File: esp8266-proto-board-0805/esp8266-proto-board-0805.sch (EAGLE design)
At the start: 13 parts

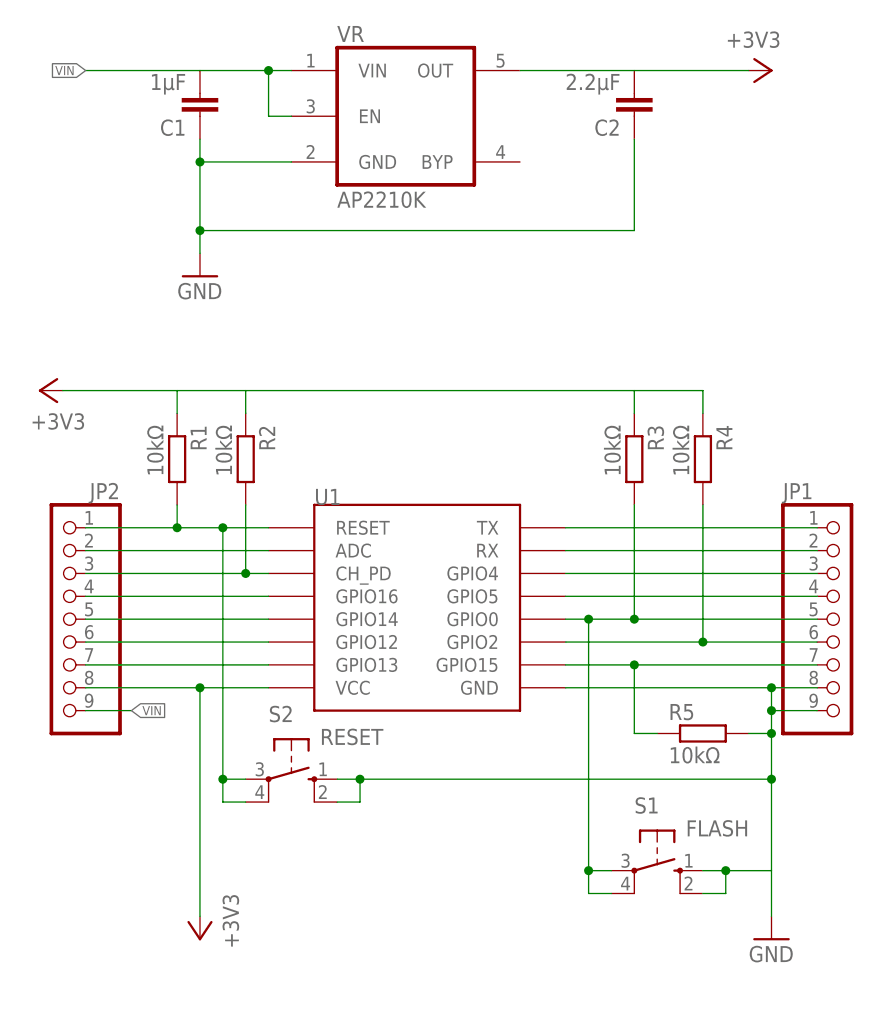
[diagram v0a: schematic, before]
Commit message: reworked 0805 version with better footprint
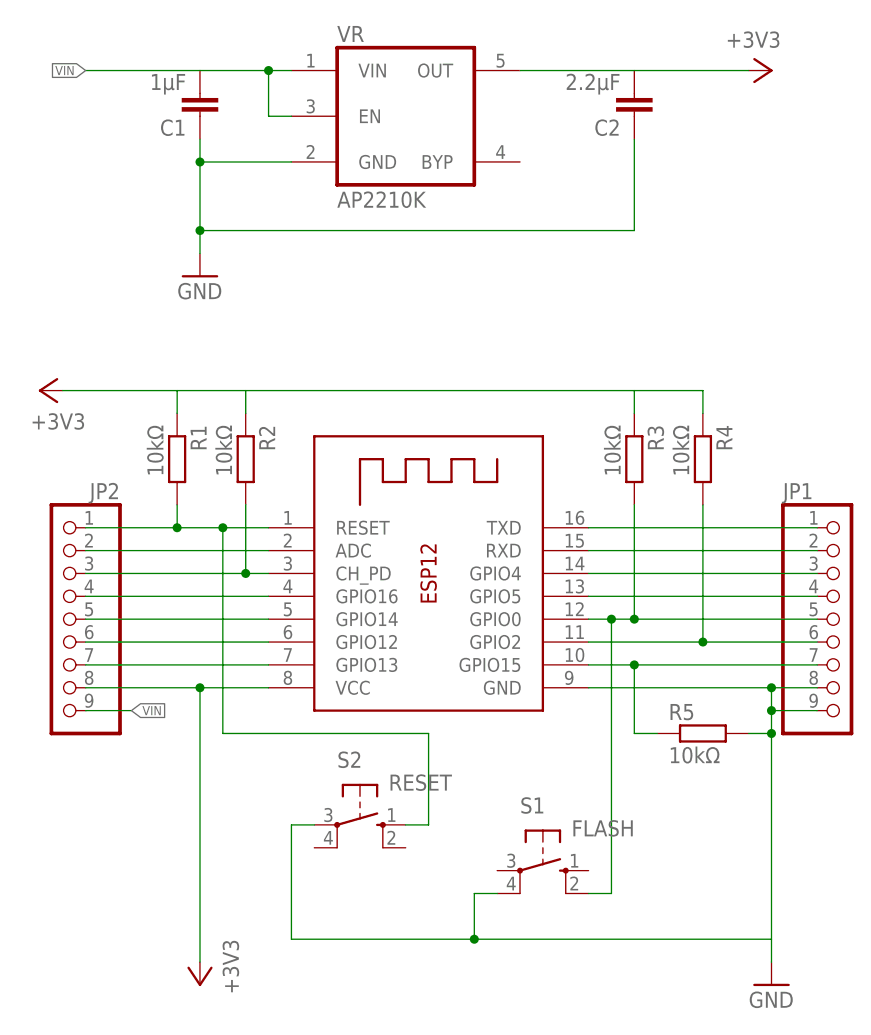
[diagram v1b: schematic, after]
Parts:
- JP1, JP2: device pinhead:PINHD-1X9 -> adafruit:PINHD-1X9
- U1: device esp8266modules:ESP12SMD -> adafruit:ESP-12
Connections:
- net GND: now also S1.P1, S2.P; no longer S1.S, S1.S1, S2.S, S2.S1
- net GPIO0: now also S1.S1; no longer S1.P, S1.P1
- net RST: now also S2.S; no longer S2.P, S2.P1
- net RX: now also U1.RXD; no longer U1.RX
- net TX: now also U1.TXD; no longer U1.TX
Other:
- moved on the sheet: S1, S2

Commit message: fixed mixed up gpio5/gpio4 in esp-lib part
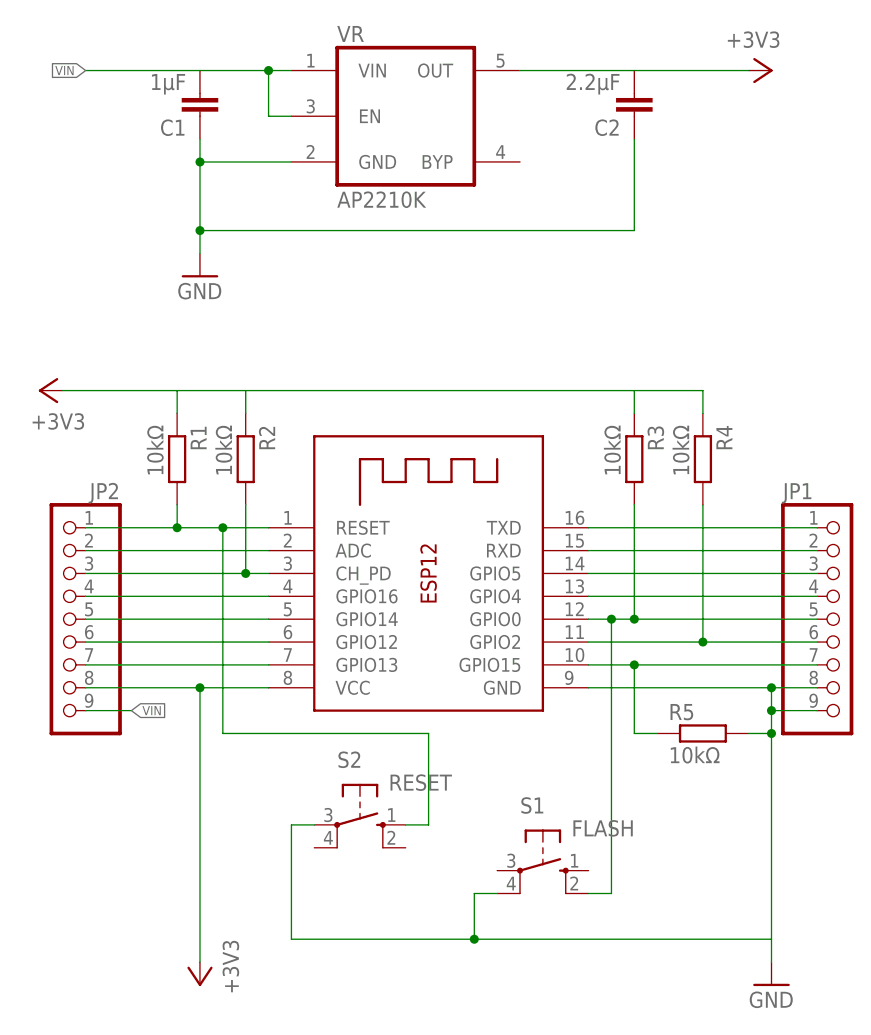
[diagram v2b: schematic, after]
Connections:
- net GPIO4: now also JP1.4; no longer JP1.3
- net GPIO5: now also JP1.3; no longer JP1.4
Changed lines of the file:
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@@
+</segment>
+</net>
+<net name="GPIO5" class="0">
+<segment>
+<pinref part="U1" gate="G$1" pin="GPIO5"/>
+<pinref part="JP1" gate="G$1" pin="3"/>
+<wire x1="104.14" y1="55.88" x2="129.54" y2="55.88" width="0.1524" layer="91"/>
 </segment>
 </net>
@@
 <segment>
 <pinref part="U1" gate="G$1" pin="GPIO4"/>
-<pinref part="JP1" gate="G$1" pin="3"/>
-<wire x1="104.14" y1="55.88" x2="129.54" y2="55.88" width="0.1524" layer="91"/>
-</segment>
-</net>
-<net name="GPIO5" class="0">
-<segment>
-<pinref part="U1" gate="G$1" pin="GPIO5"/>
 <pinref part="JP1" gate="G$1" pin="4"/>
 <wire x1="104.14" y1="53.34" x2="129.54" y2="53.34" width="0.1524" layer="91"/>
